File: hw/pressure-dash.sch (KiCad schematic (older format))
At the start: 31 parts, among them SW1 SW_Push

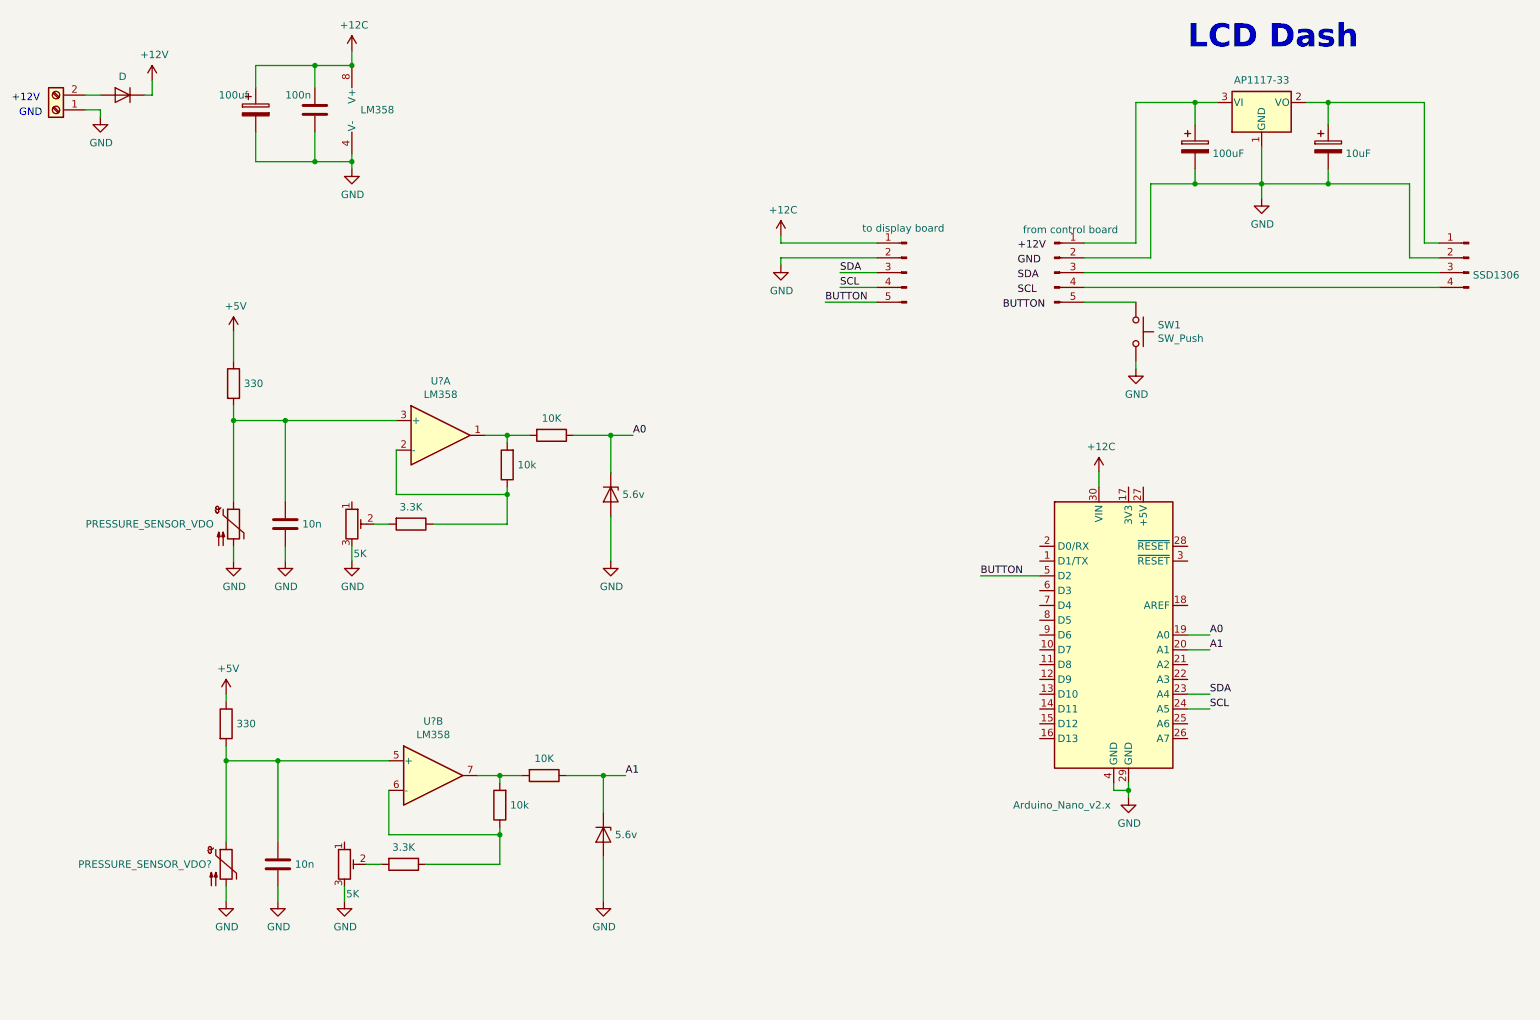
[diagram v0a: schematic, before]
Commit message: Fix schematic and calibration values
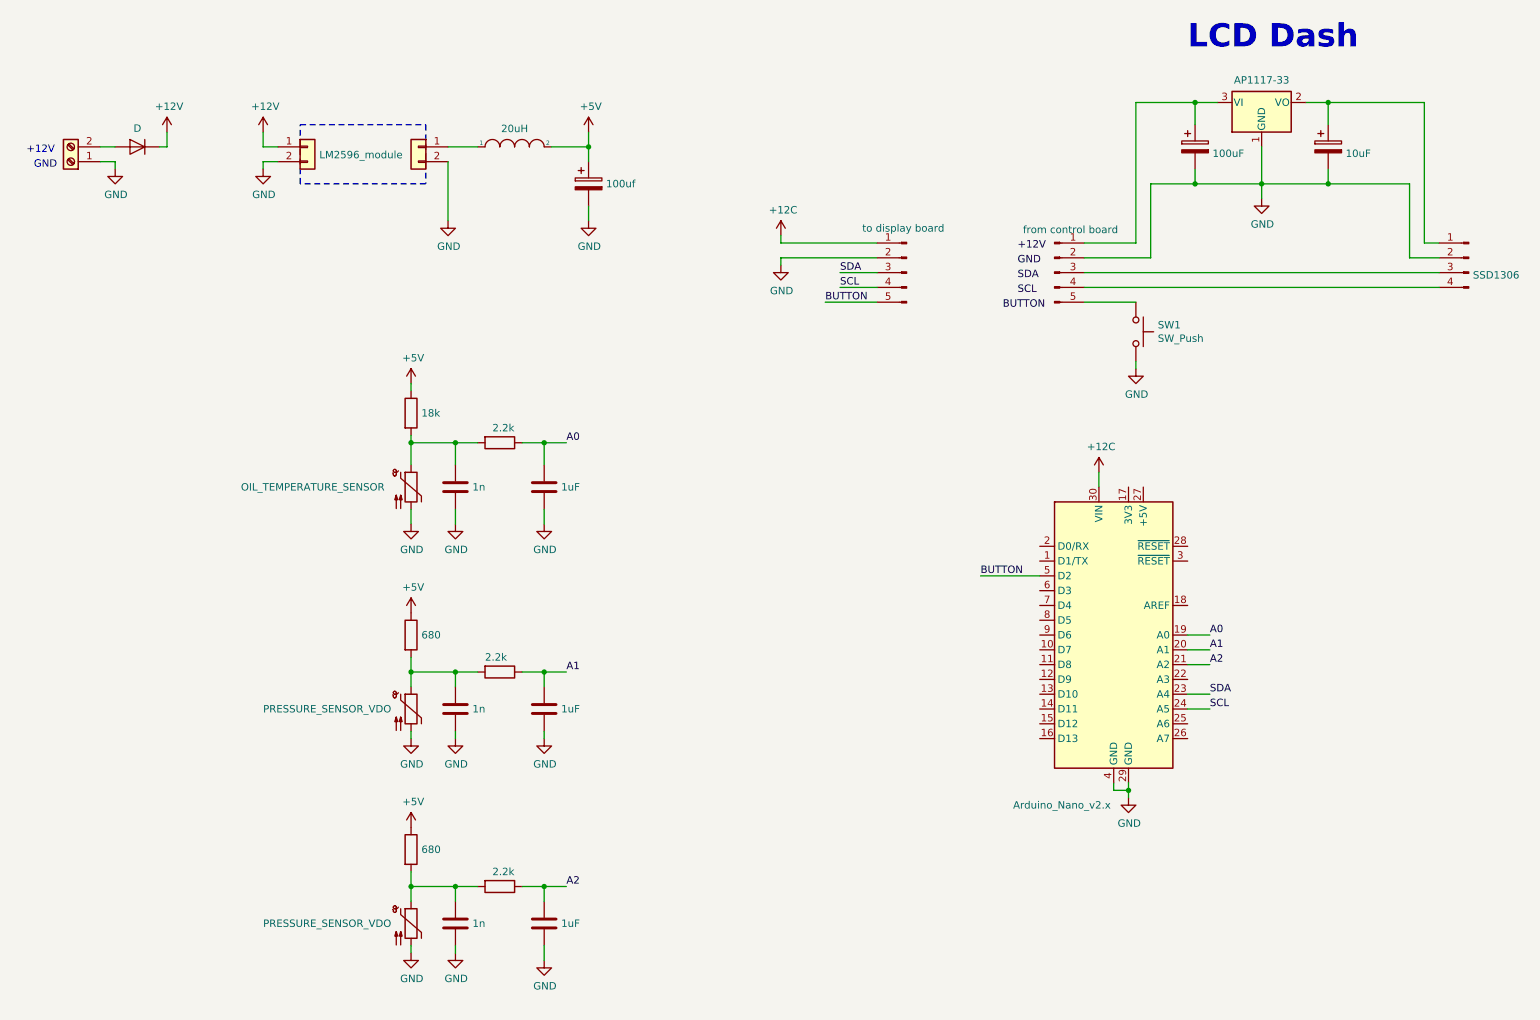
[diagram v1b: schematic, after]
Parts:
- removed C?: 100n, symbol Device:C
- removed C?: 10n, symbol Device:C
- removed C?: 100uf, symbol Device:CP
- removed D? (x2): 5.6v, symbol Device:D_Zener
- removed PRESSURE_SENSOR_VDO?: Thermistor_PTC, symbol Device:Thermistor_PTC
- removed R? (x2): 10K, symbol Device:R
- removed R? (x2): 3.3K, symbol Device:R
- removed R? (x2): 10k, symbol Device:R
- removed R?: 330, symbol Device:R
- removed RV? (x2): 5K, symbol Device:R_POT_TRIM
- removed U? (x3): LM358, symbol Amplifier_Operational:LM358
- added C? (x3): 1uF, symbol Device:C
- added C? (x2): 1n, symbol Device:C
- added C?: 100uf, symbol Device:CP
- added J?: LM2596_module, symbol Connector_Generic:Conn_01x02
- added J?: Conn_01x02, symbol Connector_Generic:Conn_01x02
- added L?: 20uH, symbol pspice:INDUCTOR
- added PRESSURE_SENSOR_VDO (x2): Thermistor_PTC, symbol Device:Thermistor_PTC
- added R? (x3): 2.2k, symbol Device:R
- added R? (x2): 680, symbol Device:R
- C?: value 10n -> 1n
- R?: value 330 -> 18k
- renumbered PRESSURE_SENSOR_VDO to OIL_TEMPERATURE_SENSOR
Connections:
- net +12V: now also J?.1 (Pin_1)
- net +5V: now also C?.1, L?.2, R?.1, R?.1
- net A0: now also C?.1, R?.1
- net A1: now also C?.1, R?.1
- net GND: now also C?.2, C?.2, C?.2, C?.2, C?.2, C?.2, J?.2 (Pin_2), J?.2 (Pin_2), PRESSURE_SENSOR_VDO.2, PRESSURE_SENSOR_VDO.2
- net A2: now reaches A?.21 (A2)
- net A2: now also C?.1, R?.1
- net at C?.1, OIL_TEMPERATURE_SENSOR.1, R?.2: now also R?.2
- new net: C?.1, PRESSURE_SENSOR_VDO.1, R?.2, R?.2 (x2)
- new net: J?.1 (Pin_1), L?.1
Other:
- moved on the sheet: OIL_TEMPERATURE_SENSOR

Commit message: Update schematic
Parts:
- removed C? (x2): 1uF, symbol Device:C
- removed C? (x2): 1n, symbol Device:C
- removed PRESSURE_SENSOR_VDO (x2): Thermistor_PTC, symbol Device:Thermistor_PTC
- removed R? (x2): 2.2k, symbol Device:R
- removed R? (x2): 680, symbol Device:R
- added C? (x2): 1uF, symbol Device:C
- added J? (x2): Screw_Terminal_01x03, symbol Connector:Screw_Terminal_01x03
- added R? (x2): 2.2k, symbol Device:R
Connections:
- net +12V: now also J?.1 (Pin_1), J?.1 (Pin_1)
- net A1: now also C?.1, R?.1
- net A2: now also C?.1, R?.1
- net GND: now also C?.2, C?.2, J?.3 (Pin_3), J?.3 (Pin_3)
- new net: J?.2 (Pin_2), R?.2 (x2)
